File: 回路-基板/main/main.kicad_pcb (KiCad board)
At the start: 2 copper layers, 63 x 63 mm, 61 parts, among them J1 Conn_01x07_Pin, J2 Conn_01x08_Pin, J3 Conn_01x08_Pin, J4 Conn_01x08_Pin, J5 Conn_01x08_Pin, J6 Conn_01x02_Pin, M1 Jumper_2_Small_Open, M2 Jumper_2_Small_Open, M3 Jumper_2_Small_Open, SW1 SW_Push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

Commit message: 修正
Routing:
- net TX=GPS: track 26.8 -> 18.1 mm
- net +3.3V: track 151.9 -> 150.6 mm
- net GND: vias 13 -> 17

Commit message: PCB進めた
発注用ファイルも作成した
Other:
- board text added: "DIO12 DIO13"
- board text added: "LED1 LED2"
- board text added: "ON"
- board text removed: "LED1 DIO12 LED2 DIO13"

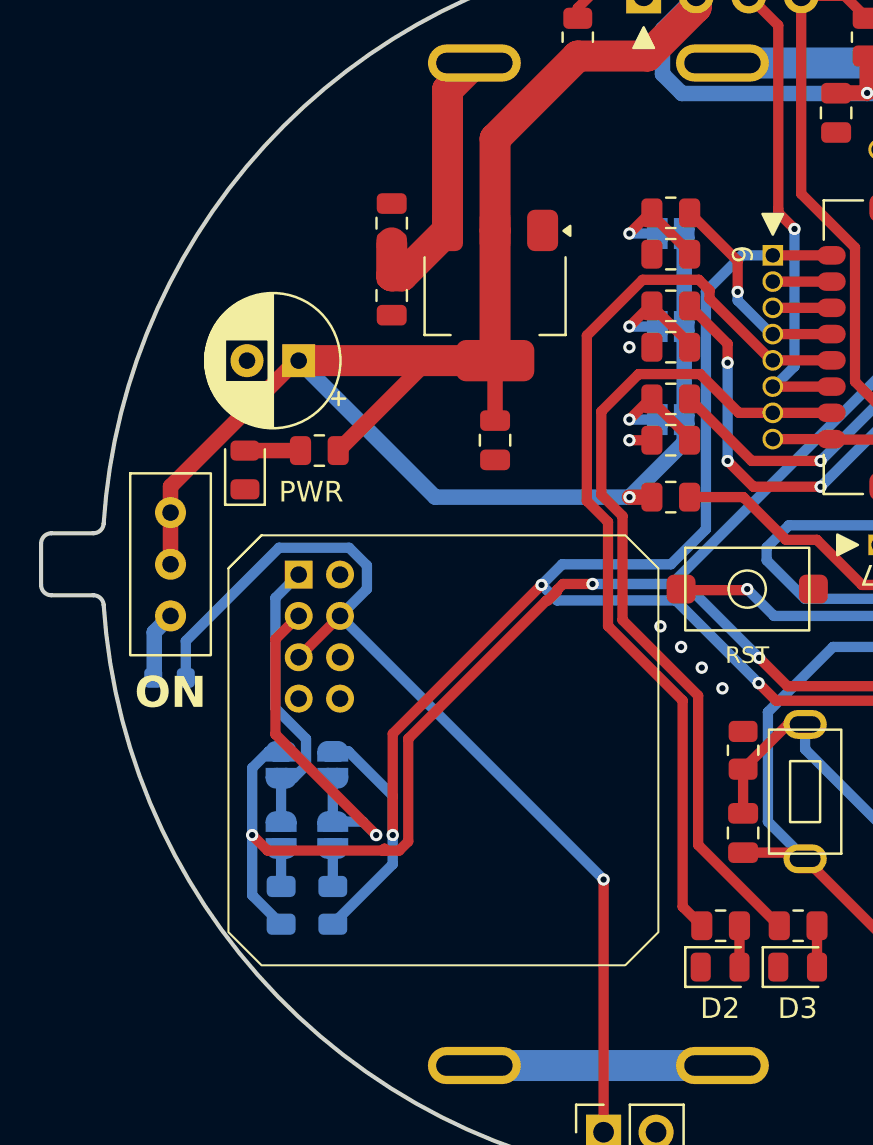
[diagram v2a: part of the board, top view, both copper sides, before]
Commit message: 子機基板のまずいところを修正して発注用ファイルを出力
一部PCBA部品が裏になってたのを表に修正した
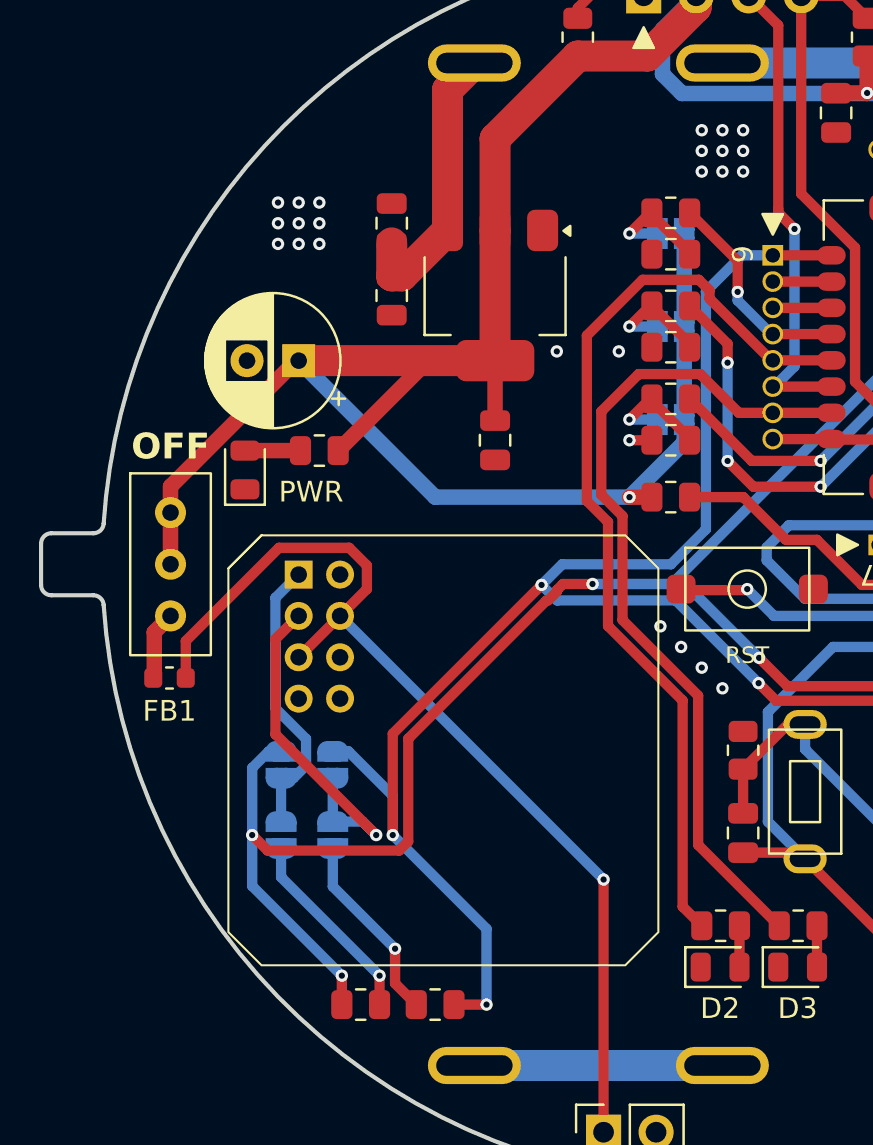
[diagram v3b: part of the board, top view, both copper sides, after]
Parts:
- FB1, R18, R19: moved to F.Cu
- moved R18 6.90 mm to (-13.9, 21.3), turned to 180 degrees
- moved R19 6.16 mm to (-17.5, 21.3), turned to 0 degrees
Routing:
- net Net-(JP7-A): track 1.84 -> 9.53 mm, vias 0 -> 1
- net Net-(JP5-A): track 1.84 -> 9.22 mm, vias 0 -> 1
- net 9: track 93.5 -> 99.6 mm, vias 3 -> 4
- net 8: track 104.2 -> 109.2 mm, vias 4 -> 5
- net GND: vias 17 -> 36
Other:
- board text added: "OFF"
- board text removed: "ON"
